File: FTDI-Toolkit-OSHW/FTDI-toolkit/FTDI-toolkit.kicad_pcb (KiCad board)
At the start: 4 copper layers, 51.3 x 20 mm, 83 parts, among them IC1 TLV70033DCKT, IC12 SN74LV1T125DCKR, IC13 74HC00BQ, IC15 TS5A3359, IC2 TLV70018DCKT, IC3 TS5A3359, IC7 SN74LV1T125DCKR, IC8 FT2232D, Y1 MQ-6.000-12-30/30/

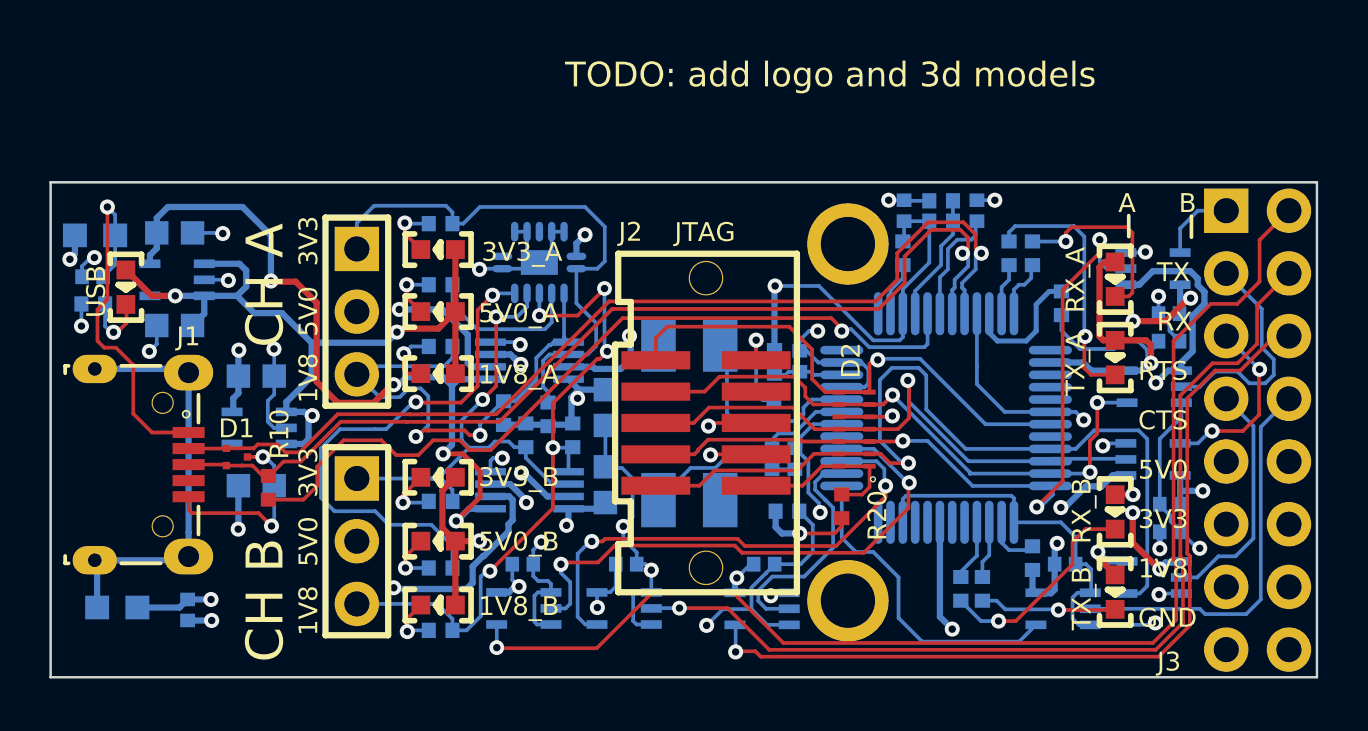
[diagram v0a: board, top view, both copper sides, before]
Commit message: Fix component orientation on PCB
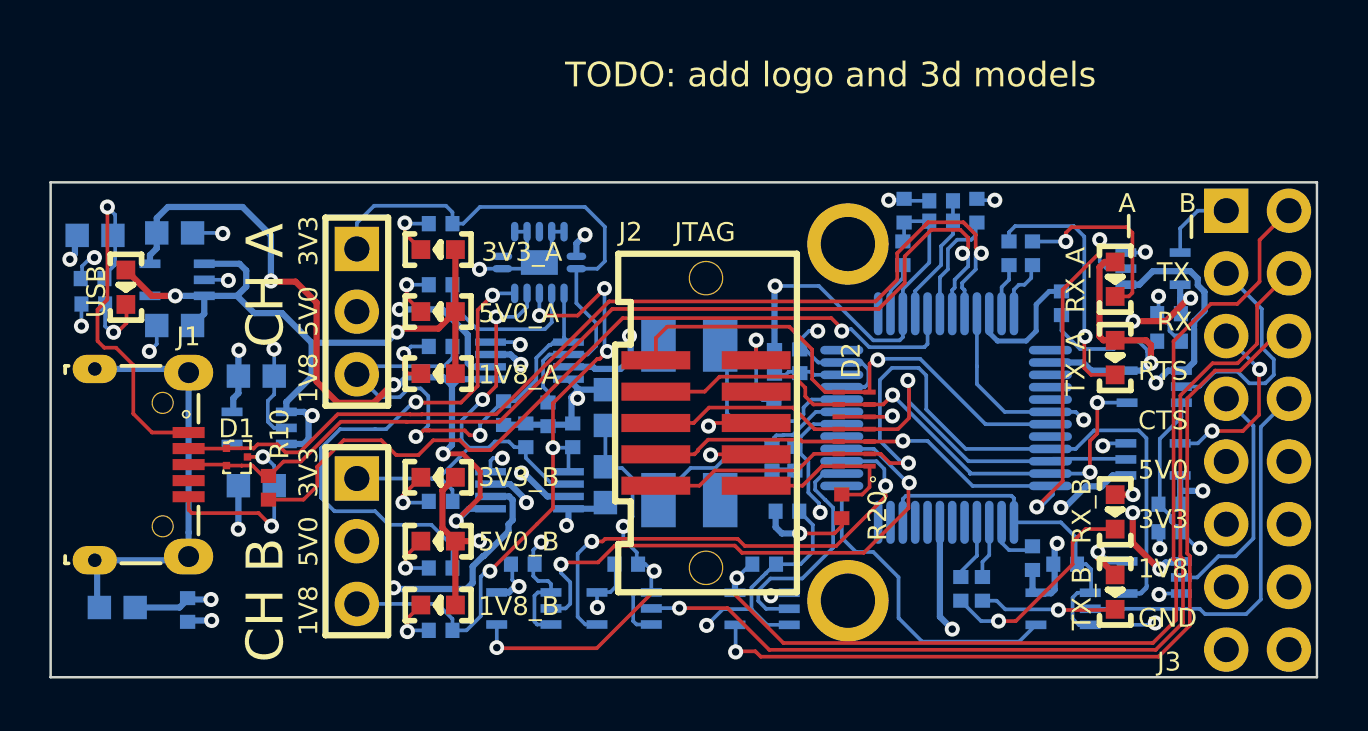
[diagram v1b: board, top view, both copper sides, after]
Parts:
- 1V8_A1, 1V8_B1, 3V3_A1, 3V3_B1, 5V0_A1, 5V0_B1, RX_A1, RX_B1, TX_A1, TX_B1, USB1: footprint LED0603 -> FTDI-toolkit:LED0603
- C1, C2, C21, C22, C5, C6, L1, L2: footprint 0603 -> FTDI-toolkit:0603
- C10, C11, C12, C13, C14, C15, C16, C17, C18, C19, C20, C3, C4, C7, C8, C9, R1, R10, R11, R12, R13, R14, R15, R16, R17, R18, R19, R2, R20, R21, R22, R23, R24, R3, R4, R5, R6, R7, R8, R9: footprint 0402 -> FTDI-toolkit:0402
- D1: footprint SOT-3 -> antmicro-footprints:SOT-3
- D2: footprint TPD6E05U06_PASS -> FTDI-toolkit:TPD6E05U06_PASS
- IC1, IC10, IC11, IC12, IC2, IC4, IC5, IC6, IC7, IC9: footprint SC70-5 -> FTDI-toolkit:SC70-5
- IC13: footprint DHVQFN14 -> FTDI-toolkit:DHVQFN14
- IC15, IC3: footprint TS5A3359 -> FTDI-toolkit:TS5A3359
- IC8: footprint LQFP-48 -> FTDI-toolkit:LQFP-48
- Y1: footprint Crystal_5x7mm -> FTDI-toolkit:Crystal_5x7mm
- moved C3 0.08 mm to (130.4, -124.6), turned to 270 degrees
- turned 1V8_A1 to 270 degrees
- turned 1V8_B1 to 270 degrees
- turned 3V3_A1 to 270 degrees
- turned 3V3_B1 to 270 degrees
- turned 5V0_A1 to 270 degrees
- turned 5V0_B1 to 270 degrees
- turned C1 to 270 degrees
- turned C10 to 90 degrees
- turned C11 to 180 degrees
- turned C12 to 180 degrees
- turned C13 to 270 degrees
- turned C14 to 270 degrees
- turned C15 to 270 degrees
- turned C16 to 270 degrees
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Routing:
- net /UART_1_CTS: track 35.6 -> 36.6 mm

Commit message: Fix component orientaton to meet IPC standards
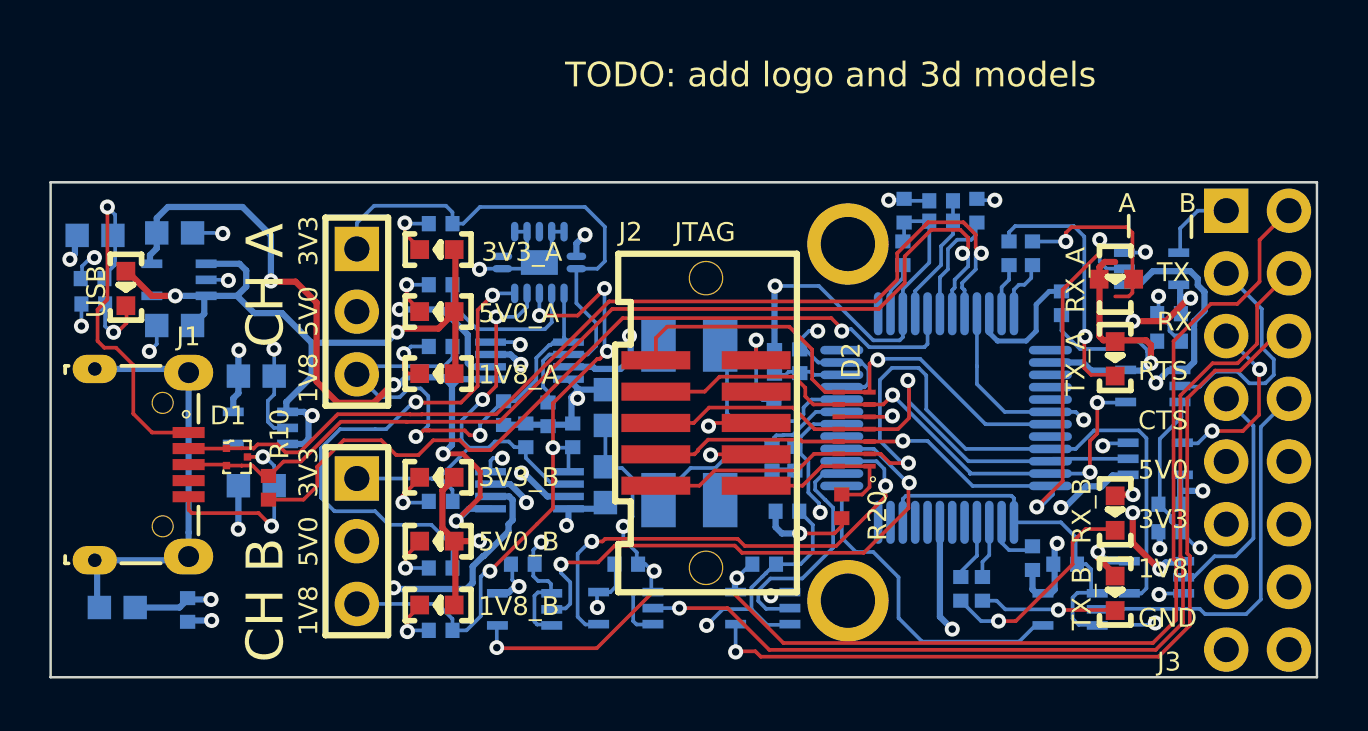
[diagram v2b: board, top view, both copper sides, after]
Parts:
- moved IC7 1.37 mm to (173.4, -117.3), turned to 0 degrees
- moved IC4 1.31 mm to (173.3, -120.2), turned to 180 degrees
- moved IC11 1.27 mm to (147.9, -111.2), turned to 180 degrees
- moved IC12 1.24 mm to (157.6, -111.2), turned to 180 degrees
- moved IC1 1.23 mm to (137.2, -118.5), turned to 180 degrees
- moved IC6 1.23 mm to (173.3, -125.0), turned to 0 degrees
- moved IC9 1.22 mm to (152.0, -111.2), turned to 180 degrees
- moved IC2 1.21 mm to (133.9, -124.5), turned to 180 degrees
- moved IC5 1.20 mm to (173.5, -112.5), turned to 180 degrees
- moved IC10 1.06 mm to (170.0, -111.2), turned to 180 degrees
- turned 1V8_A1 to 180 degrees
- turned 1V8_B1 to 180 degrees
- turned 3V3_A1 to 180 degrees
- turned 3V3_B1 to 180 degrees
- turned 5V0_A1 to 180 degrees
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
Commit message: Add 3D models
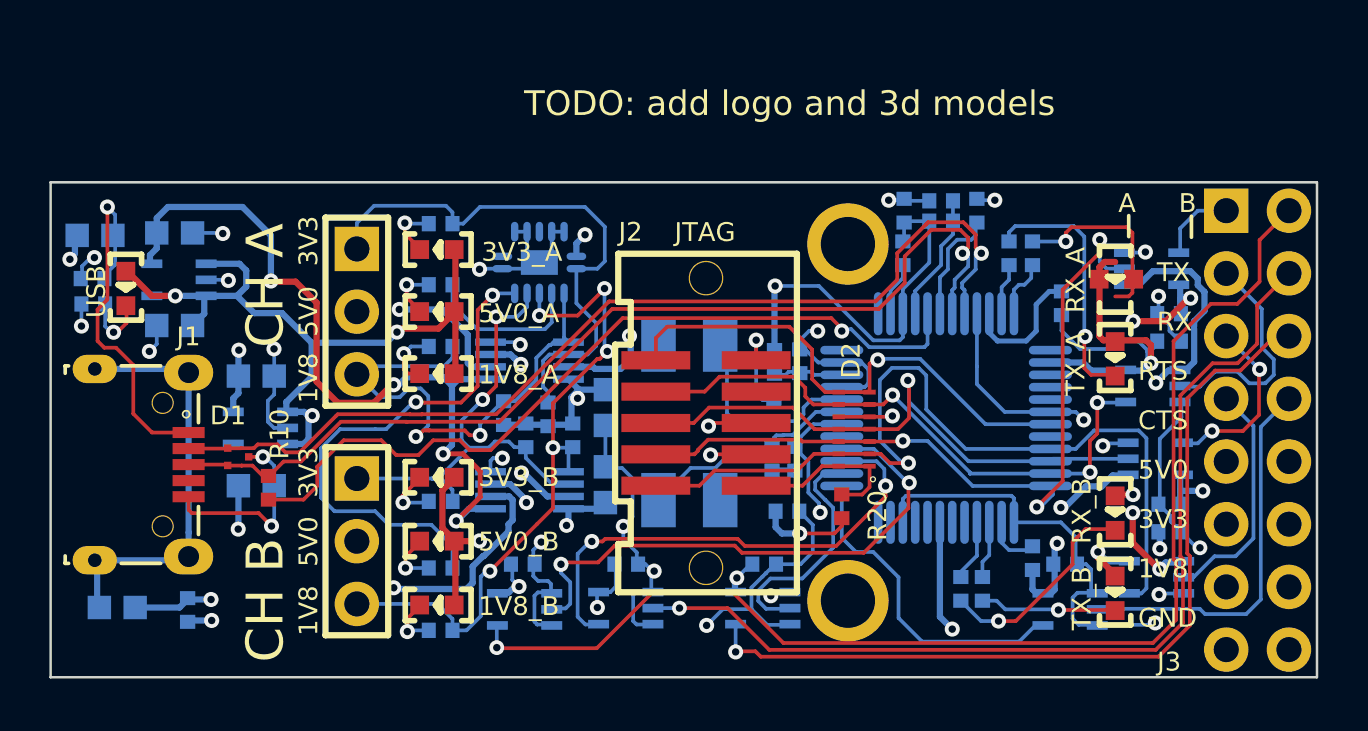
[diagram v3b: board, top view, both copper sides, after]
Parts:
- D1: footprint antmicro-footprints:SOT-3 -> FTDI-toolkit:SOT-3
- moved D1 0.05 mm to (136.3, -117.4), turned to 0 degrees

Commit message: Add logotypes to PCB
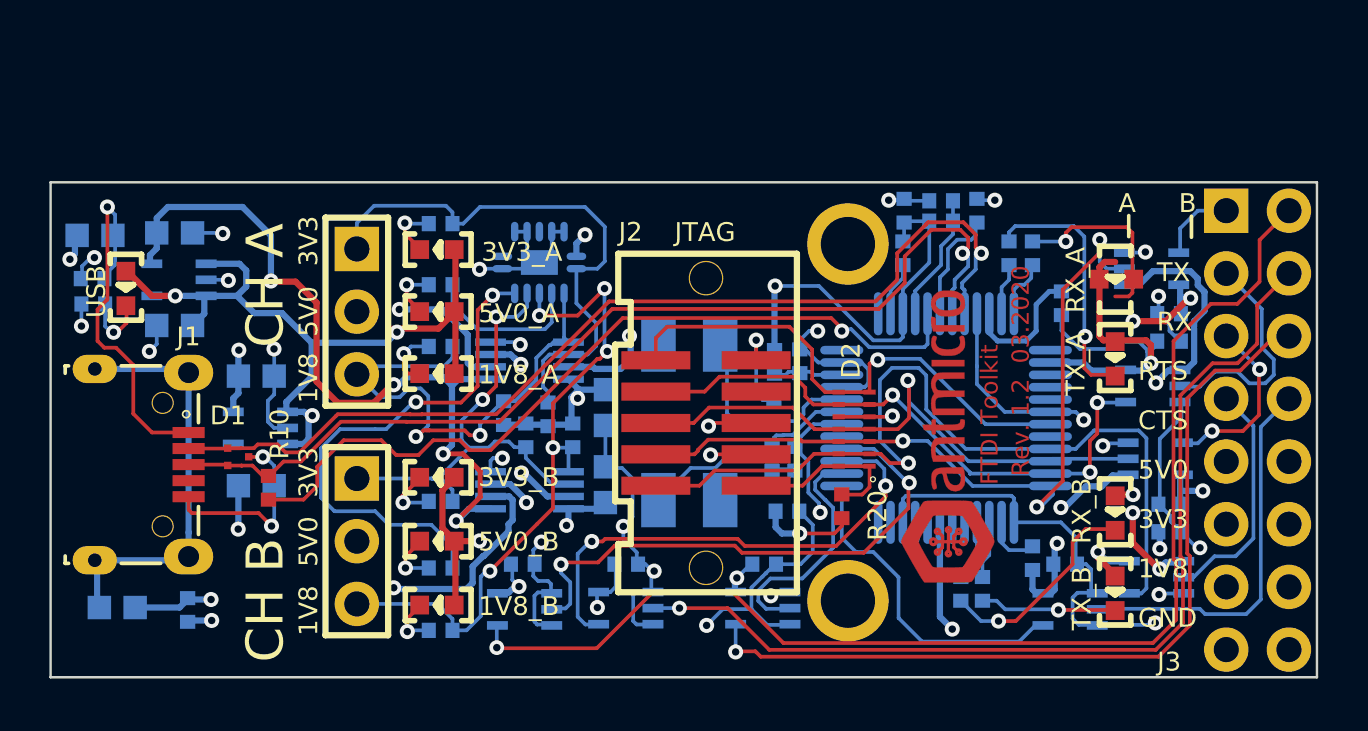
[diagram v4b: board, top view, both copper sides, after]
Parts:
- added N1: antmicro_logo, FTDI-toolkit:antmicro-logo_scaled_12mm, F.Cu at (165.1, -118.2)
- added N2: oshw_logo, FTDI-toolkit:OSHW-Logo2_7.3x6mm_SilkScreen, B.Cu at (137.7, -111.5)
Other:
- board text added: "FTDI Toolkit"
- board text added: "Rev. 1.2 03.2020"
- board text removed: "TODO: add logo and 3d models"
